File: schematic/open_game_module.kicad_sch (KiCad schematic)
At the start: 18 parts, among them J1 Expansion Port, J2 Conn_02x05_Odd_Even, U1 EPM7064S, U2 YMZ284, U3 HM62256BLP

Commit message: added models and pof from quartus
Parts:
- removed C5: 100nF, Capacitor_THT:C_Disc_D5.0mm_W2.5mm_P5.00mm, symbol Device:C
- R5: value 1k -> 470R
- R6: value 1k -> 4k7
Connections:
- net ~{CLK}: now also J1.45 (Pin_45); no longer J1.40 (Pin_40)
- net ~{RAM_CS}: now also J1.29 (Pin_29)
- net at J1.31 (Pin_31): now also R5.1, R6.2
- net DIS_MEM: no longer names the net of U1.29 (I/O)
- net DIS_MEM: no longer J1.29 (Pin_29)
- no-connect marks 26 -> 27
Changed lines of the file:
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@@
 	)
 	(junction
-		(at 118.11 119.38)
-		(diameter 0)
-		(color 0 0 0 0)
-	)
-	(junction
 		(at 224.79 100.33)
 		(diameter 0)
@@
 	)
 	(junction
+		(at 118.11 119.38)
+		(diameter 0)
+		(color 0 0 0 0)
+	)
+	(junction
 		(at 212.09 107.95)
 		(diameter 0)
@@
 	)
 	(no_connect
+		(at 96.52 161.29)
+	)
+	(no_connect
 		(at 69.85 35.56)
 	)
@@
 	)
 	(no_connect
-		(at 69.85 66.04)
-	)
-	(no_connect
 		(at 57.15 101.6)
 	)
@@
 	)
 	(no_connect
+		(at 69.85 78.74)
+	)
+	(no_connect
 		(at 257.81 83.82)
 	)
@@
 	(wire
 		(pts
-			(xy 118.11 111.76) (xy 118.11 101.6)
+			(xy 118.11 101.6) (xy 118.11 119.38)
 		)
 		(stroke
@@
 	)
 	(label "~{CLK}"
-		(at 69.85 78.74 0)
+		(at 69.85 66.04 0)
 		(effects
 			(font
@@
 		)
 	)
-	(label "DIS_MEM"
-		(at 57.15 99.06 180)
-		(effects
-			(font
-				(size 1.27 1.27)
-			)
-			(justify right bottom)
-		)
-	)
 	(label "A7"
 		(at 138.43 57.15 0)
@@
 		)
 	)
+	(label "~{RAM_CS}"
+		(at 57.15 99.06 180)
+		(effects
+			(font
+				(size 1.27 1.27)
+			)
+			(justify right bottom)
+		)
+	)
 	(label "D0"
 		(at 97.79 135.89 0)
@@
 		)
 	)
-	(label "DIS_MEM"
-		(at 96.52 161.29 0)
-		(effects
-			(font
-				(size 1.27 1.27)
-			)
-			(justify left bottom)
-		)
-	)
 	(label "A9"
 		(at 138.43 62.23 0)
@@
 			)
 		)
-		(property "Value" "1k"
+		(property "Value" "4k7"
 			(at 115.824 121.92 90)
 			(effects
@@
 			)
 		)
-		(property "Value" "1k"
+		(property "Value" "470R"
 			(at 130.81 117.094 90)
 			(effects
@@
 					(unit 1)
 				)
-			)
-		)
-	)
-	(symbol
-		(lib_id "Device:C")
-		(at 118.11 115.57 0)
-		(unit 1)
-		(exclude_from_sim no)
-		(in_bom yes)
-		(on_board yes)
-		(dnp no)
-		(property "Reference" "C5"
-			(at 108.966 113.792 0)
-			(effects
-				(font
-					(size 1.27 1.27)
-				)
-				(justify left)
-			)
-		)
-		(property "Value" "100nF"
-			(at 108.966 116.332 0)
-			(effects
-				(font
-					(size 1.27 1.27)
-				)
-				(justify left)
-			)
-		)
-		(property "Footprint" "Capacitor_THT:C_Disc_D5.0mm_W2.5mm_P5.00mm"
-			(at 119.0752 119.38 0)
-			(effects
-				(font
-					(size 1.27 1.27)
-				)
-				(hide yes)
-			)
-		)
-		(property "Datasheet" "~"
-			(at 118.11 115.57 0)
-			(effects
-				(font
-					(size 1.27 1.27)
-				)
-				(hide yes)
-			)
-		)
-		(property "Description" "Unpolarized capacitor"
-			(at 118.11 115.57 0)
-			(effects
-				(font
-					(size 1.27 1.27)
-				)
-				(hide yes)
-			)
-		)
-		(pin "2"
-		)
-		(pin "1"
-		)
-		(instances
-			(project "open_game_module"
-				(path "/133df8f4-93e5-41fe-be91-8baec47c18ae"
-					(reference "C5")
-					(unit 1)
-				)

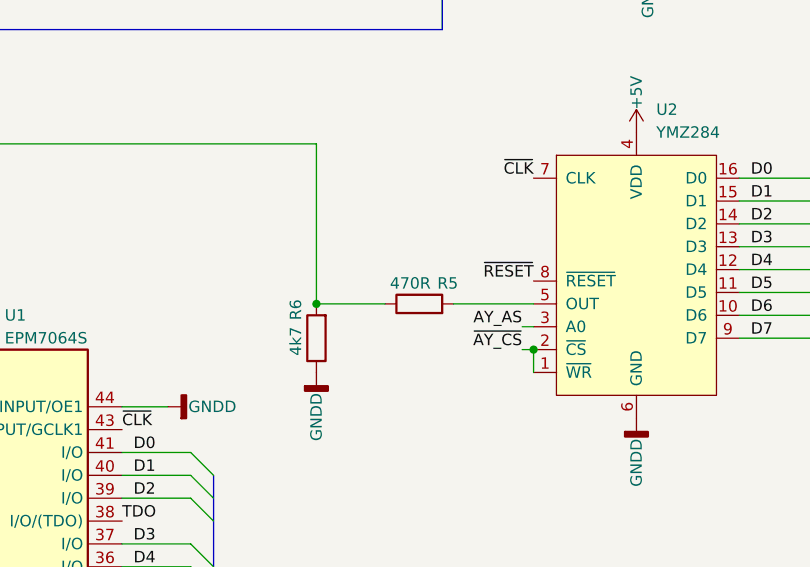
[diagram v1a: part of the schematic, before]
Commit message: fix resistor for output to 2k2 due to internal sound chip conflict issue
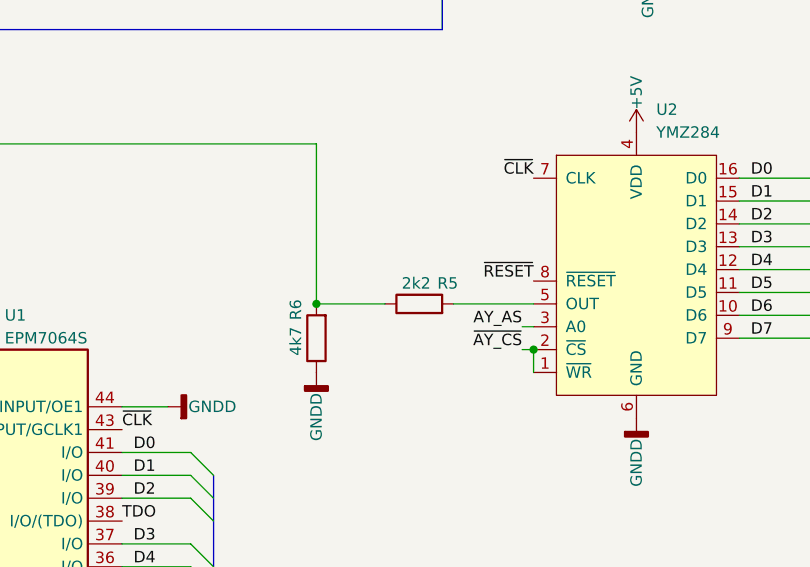
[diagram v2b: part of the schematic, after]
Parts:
- R5: value 470R -> 2k2
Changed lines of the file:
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@@
 			)
 		)
-		(property "Value" "470R"
+		(property "Value" "2k2"
 			(at 130.81 117.094 90)
 			(effects
